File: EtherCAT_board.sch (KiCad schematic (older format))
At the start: 2 parts

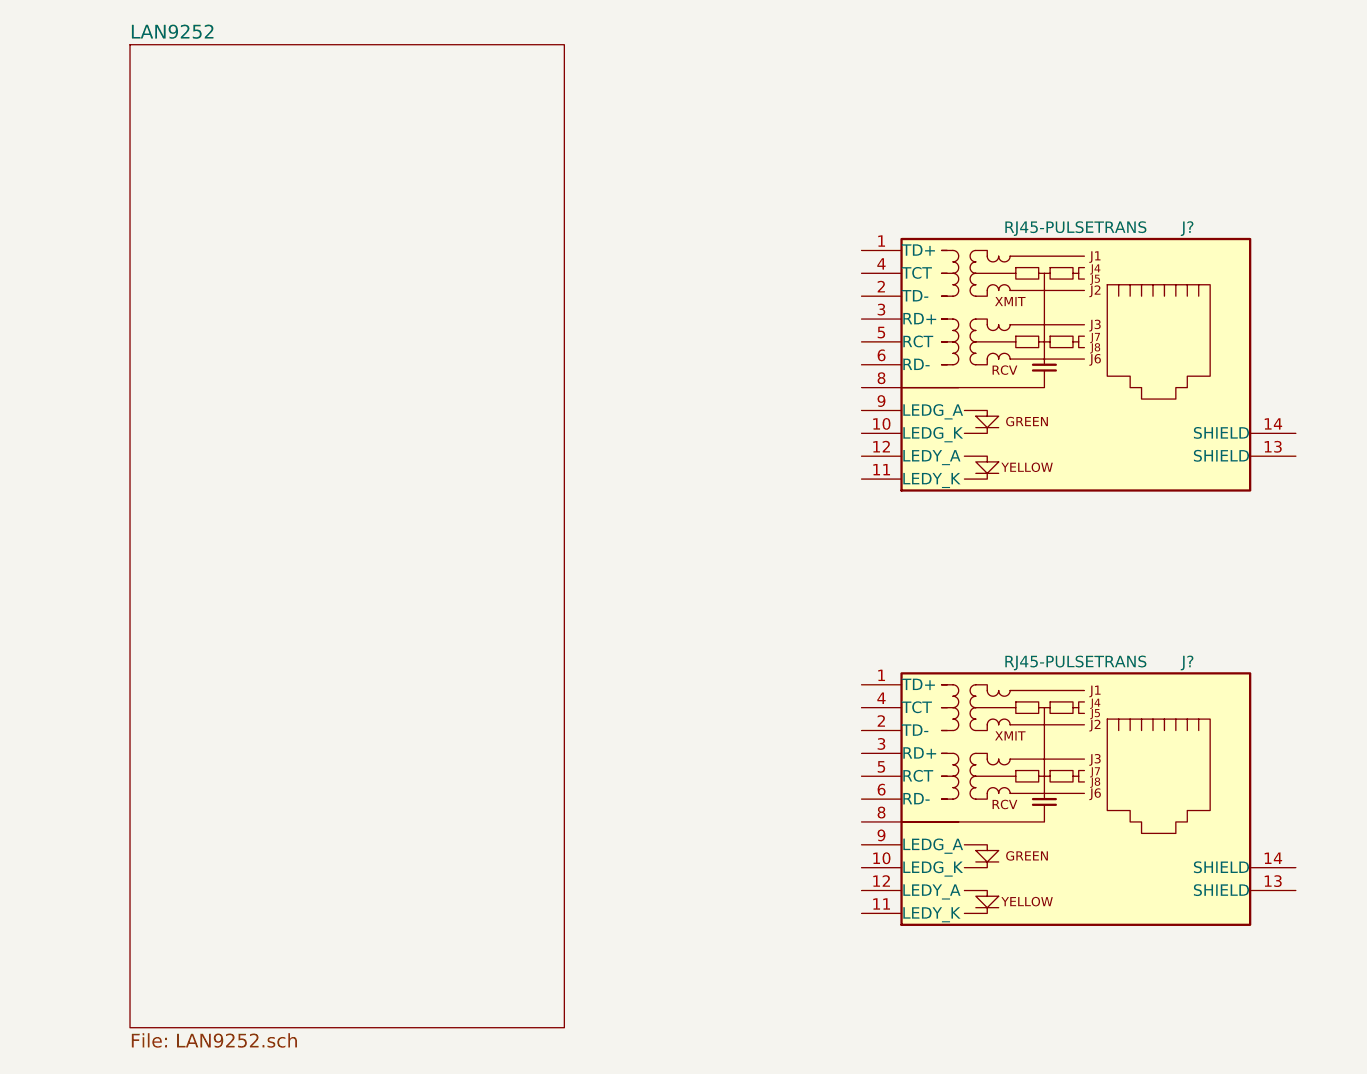
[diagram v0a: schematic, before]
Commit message: LAN9252まわりの配線した
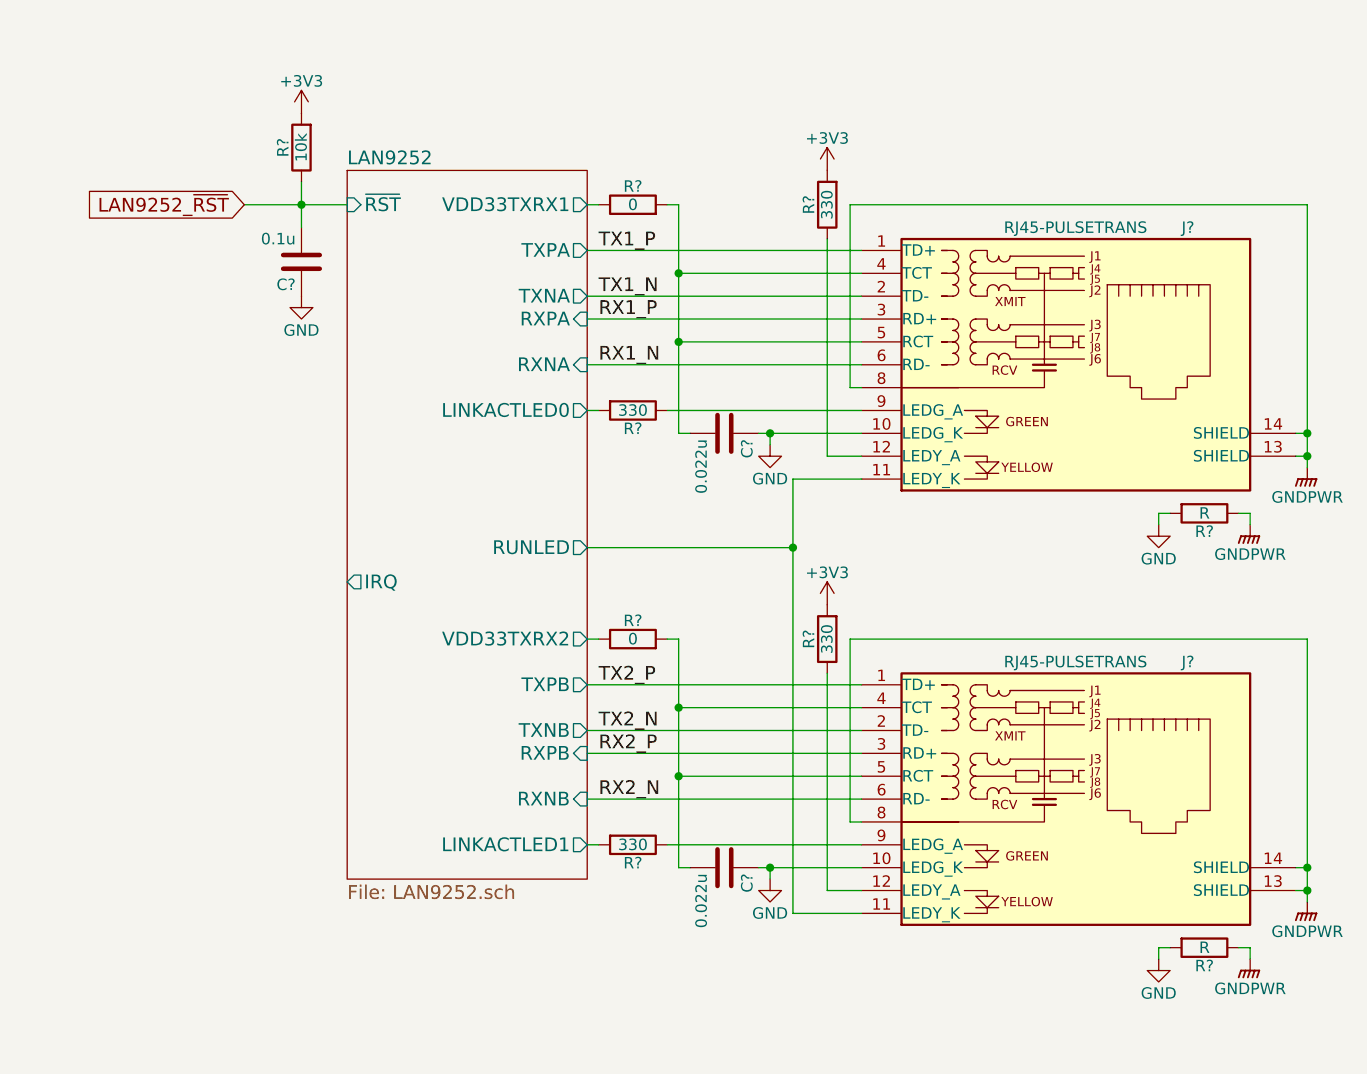
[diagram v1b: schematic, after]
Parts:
- removed J? (x2): RJ45-PULSETRANS, symbol RJ45-PULSETRANS
- added C? (x2): 0.022u, symbol C
- added C?: 0.1u, symbol C
- added J? (x2): RJ45-PULSETRANS, symbol RJ45-PULSETRANS
- added R? (x4): 330, symbol R
- added R? (x2): R, symbol R
- added R? (x2): 0, symbol R
- added R?: 10k, symbol R
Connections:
- new net: J?.12 (LEDY_A), R?.1 (x2)
- new net: C?.2, J?.4 (TCT), J?.5 (RCT), R?.2 (x2)
- new net: J?.9 (LEDG_A), R?.1 (x2)
- new net +3V3: R?.2, R?.2, R?.2
- new net GND: C?.1, C?.1, C?.1, J?.10 (LEDG_K), J?.10 (LEDG_K), R?.2, R?.2
- new net GNDPWR: J?.13 (SHIELD), J?.13 (SHIELD), J?.14 (SHIELD), J?.14 (SHIELD), J?.8, J?.8, R?.1, R?.1
- new net LAN9252/LINKACTLED0: R?.2
- new net LAN9252/LINKACTLED1: R?.2
- new net LAN9252/RUNLED: J?.11 (LEDY_K), J?.11 (LEDY_K)
- new net LAN9252/VDD33TXRX1: R?.1
- new net LAN9252/VDD33TXRX2: R?.1
- new net LAN9252_~RST: C?.2, R?.1
- new net RX1_N: J?.6 (RD-)
- new net RX1_P: J?.3 (RD+)
- new net RX2_N: J?.6 (RD-)
- new net RX2_P: J?.3 (RD+)
- new net TX1_N: J?.2 (TD-)
- new net TX1_P: J?.1 (TD+)
- new net TX2_N: J?.2 (TD-)
- new net TX2_P: J?.1 (TD+)

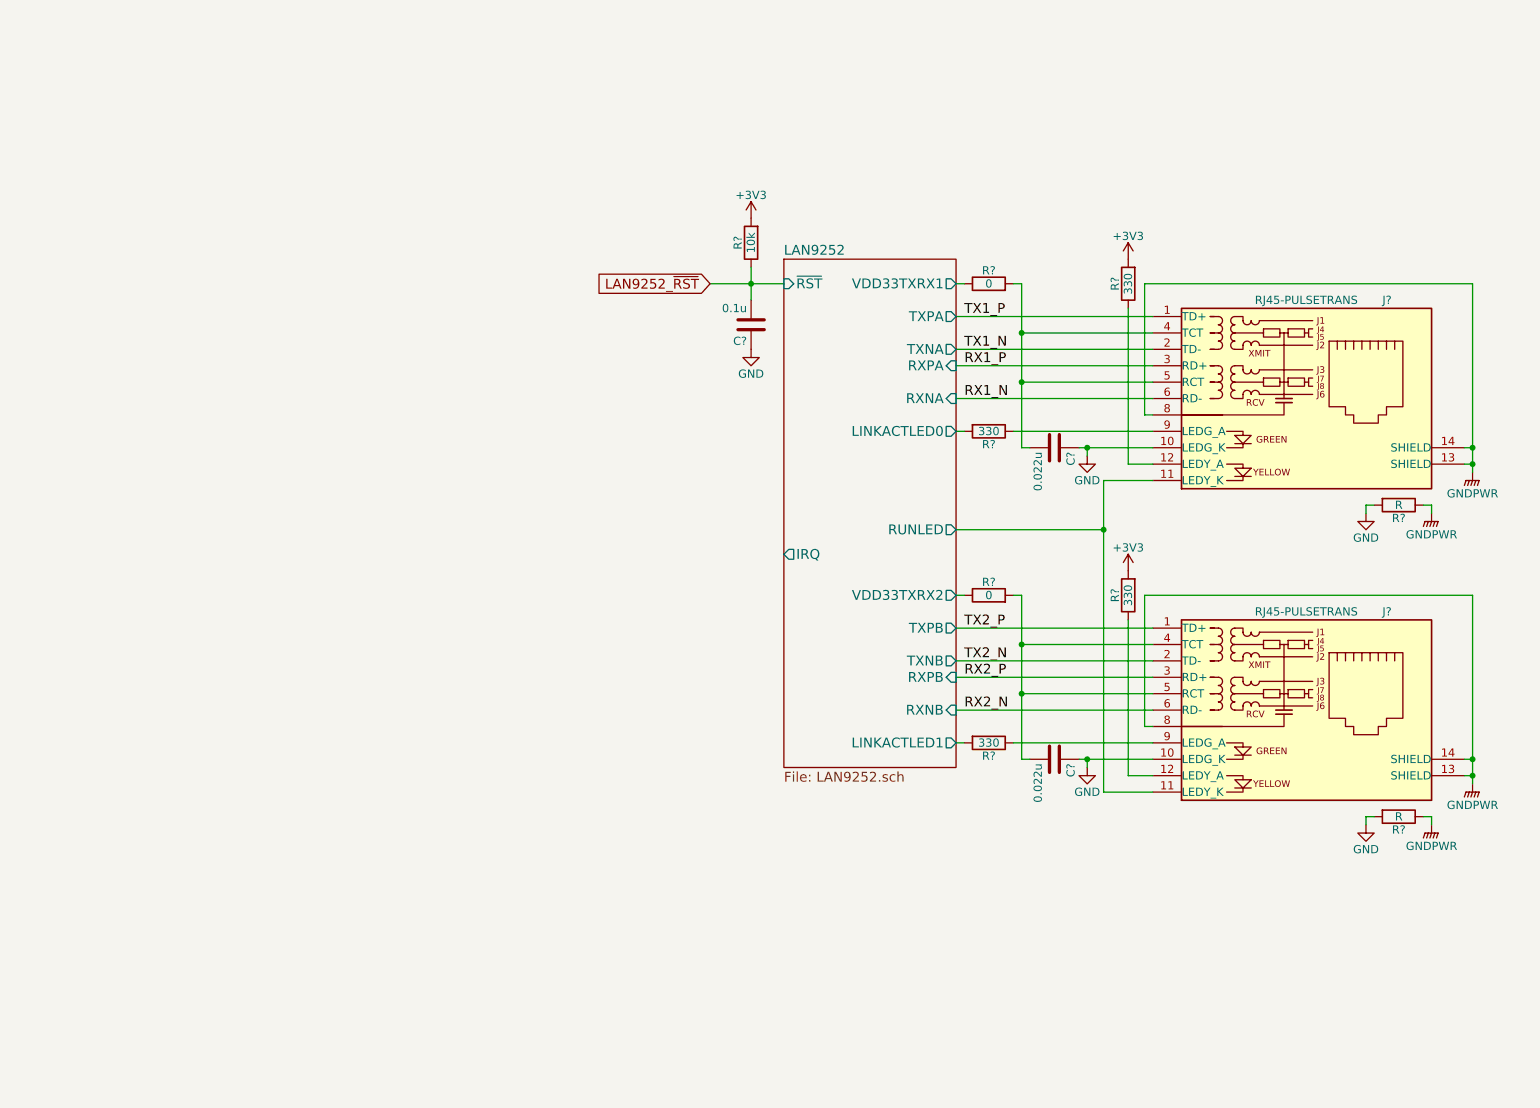
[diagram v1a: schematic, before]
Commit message: スイッチ，LEDの配線 電源回路追加 アノテーション
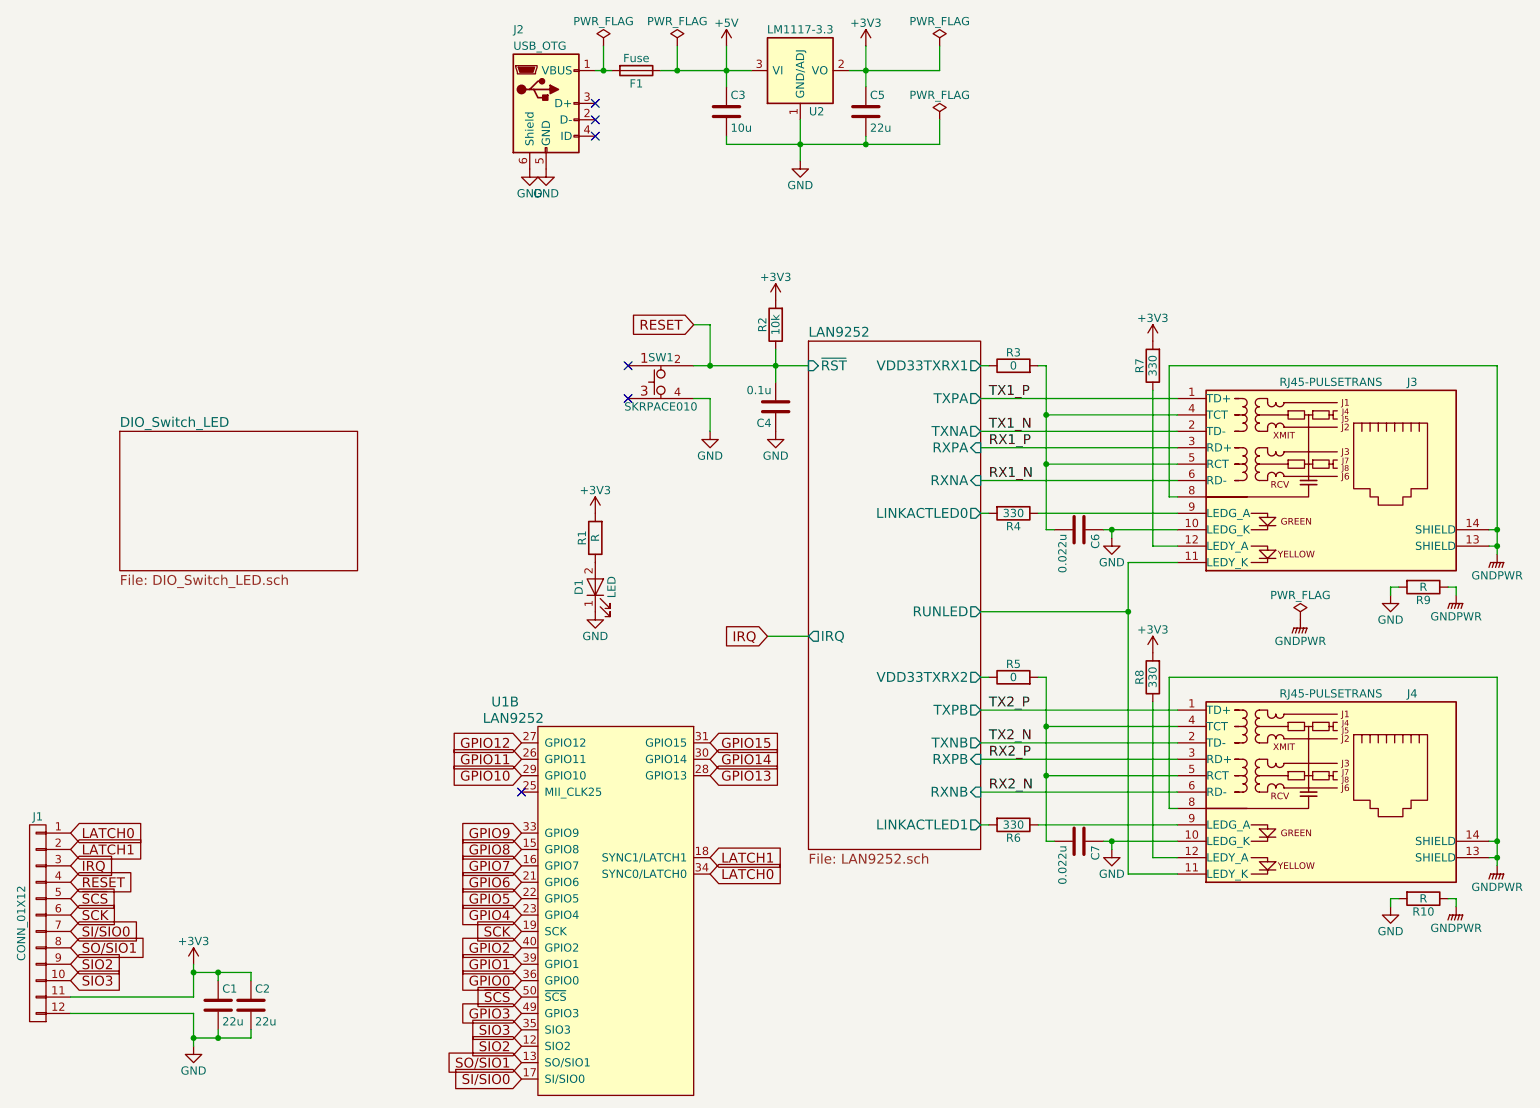
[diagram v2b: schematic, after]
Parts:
- added C1, C2, C5: 22u, symbol C
- added C3: 10u, symbol C
- added D1: LED, symbol LED
- added F1: Fuse, symbol Fuse
- added J1: CONN_01X12, symbol CONN_01X12
- added J2: USB_OTG, symbol USB_OTG
- added R1: R, symbol R
- added SW1: SKRPACE010, symbol SKRPACE010
- added U1: LAN9252, symbol LAN9252
- added U2: LM1117-3.3, symbol LM1117-3.3
- gave numbers to parts that had none: 14
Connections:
- net +3V3: now also C1.1, C2.1, C5.1, J1.11 (P11), R1.2, U2.2 (VO), U2.4 (VO)
- net GND: now also C1.2, C2.2, C3.2, C5.2, D1.1 (K), J1.12 (P12), J2.5 (GND), J2.6 (Shield), SW1.4, U2.1 (GND/ADJ)
- net LAN9252_~RST renamed RESET
- net RESET: now also J1.4 (P4), SW1.2
- new net: F1.2, J2.1 (VBUS)
- new net: D1.2 (A), R1.1
- new net +5V: C3.1, F1.1, U2.3 (VI)
- new net GPIO0: U1.36 (GPIO0)
- new net GPIO1: U1.39 (GPIO1)
- new net GPIO10: U1.29 (GPIO10)
- new net GPIO11: U1.26 (GPIO11)
- new net GPIO12: U1.27 (GPIO12)
- new net GPIO13: U1.28 (GPIO13)
- new net GPIO14: U1.30 (GPIO14)
- new net GPIO15: U1.31 (GPIO15)
- new net GPIO2: U1.40 (GPIO2)
- new net GPIO3: U1.49 (GPIO3)
- new net GPIO4: U1.23 (GPIO4)
- new net GPIO5: U1.22 (GPIO5)
- new net GPIO6: U1.21 (GPIO6)
- new net GPIO7: U1.16 (GPIO7)
- new net GPIO8: U1.15 (GPIO8)
- new net GPIO9: U1.33 (GPIO9)
- new net IRQ: J1.3 (P3)
- new net LATCH0: J1.1 (P1), U1.34 (SYNC0/LATCH0)
- new net LATCH1: J1.2 (P2), U1.18 (SYNC1/LATCH1)
- new net SCK: J1.6 (P6), U1.19 (SCK)
- new net SI/SIO0: J1.7 (P7), U1.17 (SI/SIO0)
- new net SIO2: J1.9 (P9), U1.12 (SIO2)
- new net SIO3: J1.10 (P10), U1.35 (SIO3)
- new net SO/SIO1: J1.8 (P8), U1.13 (SO/SIO1)
- new net ~SCS: J1.5 (P5), U1.50 (~SCS)
- no-connect marks 0 -> 6
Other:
- moved on the sheet: C4, C6, C7, J3, J4, R10, R2, R3, R4, R5, R6, R7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
